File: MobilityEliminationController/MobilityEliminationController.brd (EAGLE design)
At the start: 57.1 x 63.5 mm, 94 parts, among them Q1 INFINEON_2N7002_DW, Q2 INFINEON_2N7002_DW, Q3 BS250F, Q4 BS250F, Q5 INFINEON_2N7002_DW, Q6 INFINEON_2N7002_DW, U1 MSP430F5521/5/7/9_PN80, U2 SN74LV74, U3 SN74LV08

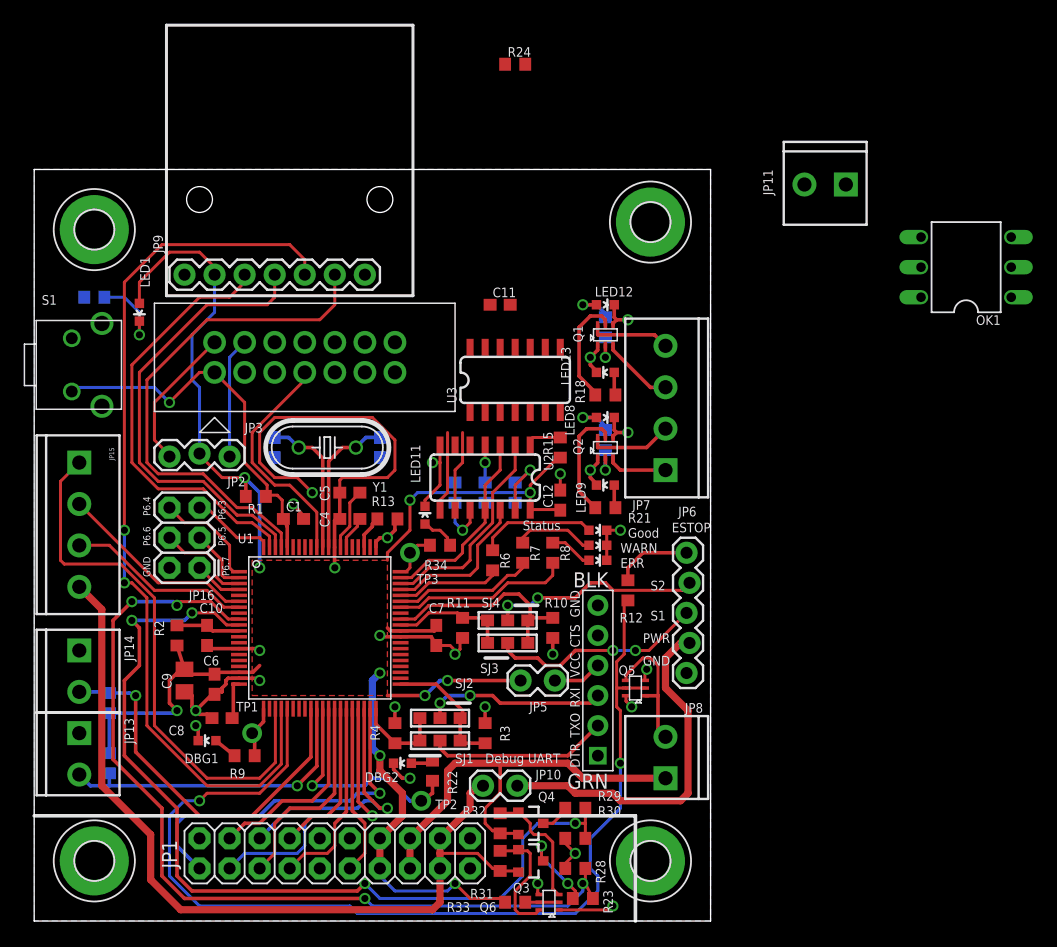
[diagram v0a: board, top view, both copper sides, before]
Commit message: Mob/Elim controller ready for fab
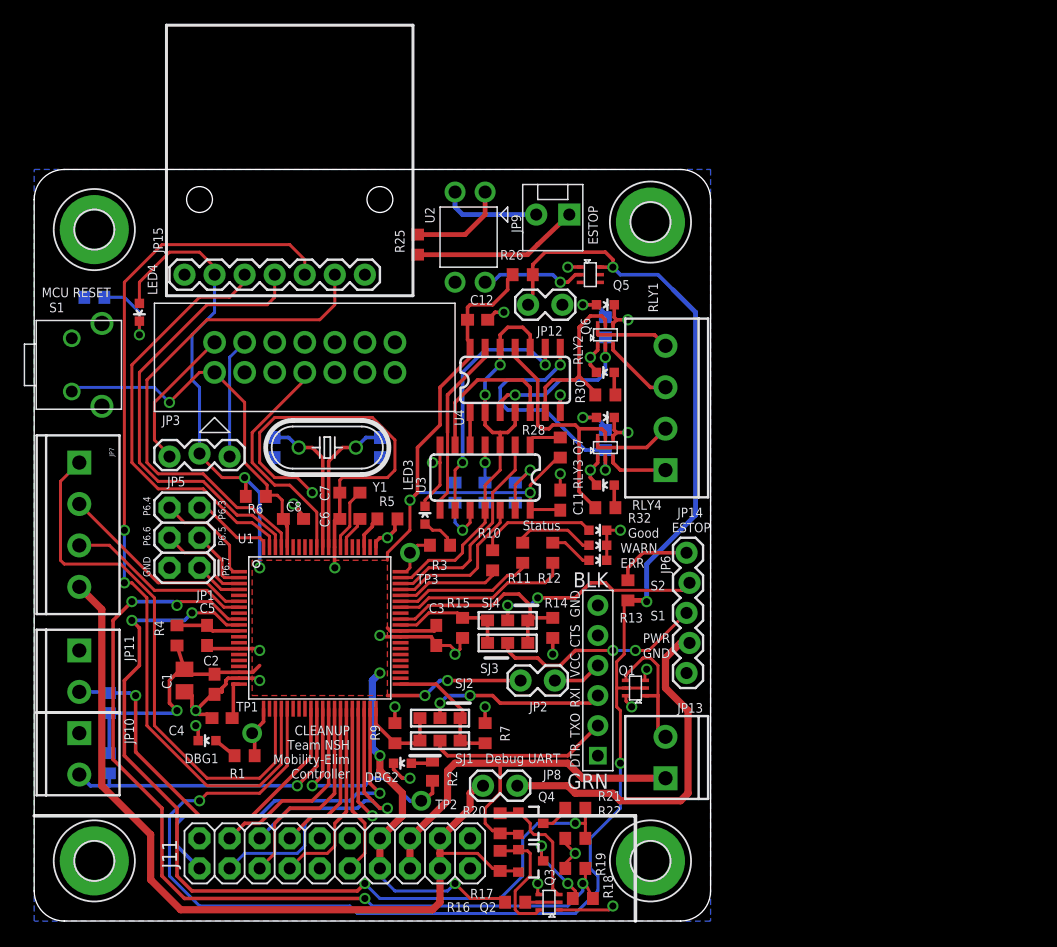
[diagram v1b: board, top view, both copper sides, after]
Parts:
- removed JP16: (no value), SparkFun-Connectors:2X3
- removed LED12, LED13: (no value), SparkFun-LED:LED-0603
- removed OK1: 4N35, optocoupler:DIL06
- removed R35: 1k, rcl:R0603
- added J11: M10X2, SparkFun-Connectors:2X10
- added JP12: M02LOCK, SparkFun-Connectors:1X02_LOCK
- added LED6: Status: Yellow, SparkFun-LED:LED-0603
- added LED7: Status: Red, SparkFun-LED:LED-0603
- added Q7: INFINEON_2N7002_DW, npol-discrete:INFINEON_SOT363
- added R19: 100k, rcl:R0603
- added R25: 620, rcl:R0603
- added U4: SN74LV08, npol-digital:TI_D_R-PDSO-G14_SOIC14
- C1: value 1nF -> 10uF; device rcl:C0603 -> rcl:C0805
- C10: value 0.1uF -> 1nF
- C2, C3: value 1nF -> 0.1uF
- C4: value 220nF -> 470nF
- C5: value 220nF -> 0.1uF
- C6, C7: value 0.1uF -> 220nF
- C8: value 470nF -> 1nF
- C9: value 10uF -> 1nF; device rcl:C0805 -> rcl:C0603
- JP1: value M10X2 -> (none); device SparkFun-Connectors:2X10 -> SparkFun-Connectors:2X3
- JP10: value M02LOCK -> M023.5MM; device SparkFun-Connectors:1X02_LOCK -> SparkFun-Connectors:SCREWTERMINAL-3.5MM-2
- JP14: value M023.5MM -> (none); device SparkFun-Connectors:SCREWTERMINAL-3.5MM-2 -> SparkFun-Connectors:SCREWTERMINAL-3.5MM-4
- JP15: device SparkFun-Connectors:SCREWTERMINAL-3.5MM-4 -> SparkFun-Connectors:1X07
- JP2: value (none) -> M02LOCK; device SparkFun-Connectors:1X03_LOCK -> SparkFun-Connectors:1X02_LOCK
- JP5: value M02LOCK -> (none); device SparkFun-Connectors:1X02_LOCK -> SparkFun-Connectors:1X03_LOCK
- JP8: value M023.5MM -> M02LOCK; device SparkFun-Connectors:SCREWTERMINAL-3.5MM-2 -> SparkFun-Connectors:1X02_LOCK
- JP9: value (none) -> M02POLAR_LOCK; device SparkFun-Connectors:1X07 -> SparkFun-Connectors:MOLEX-1X2_LOCK
- LED1: value 3V3 OK -> Status: Red
- LED10, LED11: value Status: Red -> (none)
- LED2: value Status: Green -> Status: Red
- LED3: value Status: Yellow -> Status: Red
- LED4: value Status: Red -> 3V3 OK
- LED5: value Status: Red -> Status: Green
- R1: value 47k -> 330
- R10, R11, R3: value 10k -> 330
- R12, R2: value 0 -> 330
- R13: value 1M -> 0
- R14, R15, R16, R17: value 0 -> 10k
- R18, R21: value 1k -> 100k
- R20: value 1k -> 10k
- R22, R7, R9: value 330 -> 10k
- R23: value 100k -> 10k
- R24: value 620 -> 10k
- R27, R33, R4: value 10k -> 0
- R28: value 100k -> 0
- R29: value 100k -> 1k
- R30, R31, R32: value 10k -> 1k
- R34: value 330 -> 0
- R5: value 330 -> 1M
- R6: value 330 -> 47k
- U2: value SN74LV74 -> LTV-817; device npol-digital:TI_D_R-PDSO-G14_SOIC14 -> npol-digital:LITEON_DIL04_.3
- U3: value SN74LV08 -> SN74LV74
- moved JP11 75.8 mm to (3.81, 22.9), turned to 270 degrees
- moved R24 63.9 mm to (6.35, 18.4), flipped to the bottom, turned to 270 degrees
- moved R26 54.1 mm to (41.3, 54.6), flipped to the top, turned to 0 degrees
- moved JP14 51.8 mm to (53.3, 38.1), turned to 90 degrees
- moved JP13 49.7 mm to (53.3, 12.1), turned to 90 degrees
- moved JP7 49.5 mm to (3.81, 38.7), turned to 270 degrees
- moved Q6 48.2 mm to (48.3, 49.5), turned to 0 degrees
- moved R8 44.3 mm to (5.08, 52.7), flipped to the bottom, turned to 180 degrees
- moved LED4 44.0 mm to (8.89, 51.4), turned to 180 degrees
- moved R18 42.6 mm to (46.4, 1.91)
- moved R23 41.6 mm to (6.35, 13.3), flipped to the bottom, turned to 90 degrees
- moved R29 40.7 mm to (48.3, 50.2), flipped to the bottom, turned to 270 degrees
- moved Q2 38.7 mm to (43.5, 1.59), turned to 90 degrees
- moved R30 37.6 mm to (48.3, 44.5), turned to 180 degrees
- moved LED5 37.5 mm to (47.6, 33.0), turned to 270 degrees
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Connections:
- removed net N$38: OK1.1, R24.1
- new net ESTOP_LOCAL_INV: Q5.2, U2.4
- net +12V: now also J11.15, J11.16, JP13.1, R20.2; no longer JP1.15, JP1.16, JP8.1, R32.2
- net +3V3: now also C1.1, C2.1, C3.1, J11.13, J11.14, JP15.2, JP2.1, JP5.2, LED4.A, R23.2, R24.2, R26.1, R28.1, R34.1, R4.2, R6.2, U4.14; no longer C6.1, C7.1, C9.1, JP1.13, JP1.14, JP2.2, JP5.1, JP9.2, LED1.A, R1.2, R14.2, R15.1, R17.1, R2.2, R26.2, U2.14
- net +5V: now also J11.17, J11.18, JP7.4, JP8.2, R17.2; no longer JP1.17, JP1.18, JP10.2, JP15.4, R31.2
- net 12VSENSE: now also R21.1, R22.2; no longer R29.1, R30.2
- net 5VSENSE: now also R18.1, R19.2; no longer R23.1, R28.2
- net AVCC: now also C5.1, R4.1; no longer C10.1, R2.1
- net CAN_/CS: now also J11.4; no longer JP1.4
- net CAN_/INT: now also J11.5; no longer JP1.5
- net CAN_/RESET: now also J11.2; no longer JP1.2
- net CAN_/RX0BF: now also J11.8; no longer JP1.8
- net CAN_/RX1BF: now also J11.7; no longer JP1.7
- net CAN_/TX0RTS: now also J11.12; no longer JP1.12
- net CAN_/TX1RTS: now also J11.9; no longer JP1.9
- net CAN_/TX2RTS: now also J11.10; no longer JP1.10
- net CAN_MISO: now also J11.6; no longer JP1.6
- net CAN_MOSI: now also J11.3; no longer JP1.3
- net CAN_SCK: now also J11.1; no longer JP1.1
- net CAN_STBY: now also J11.11; no longer JP1.11
- net DBG_LED1: now also R1.2; no longer R9.2
- net DBG_LED2: now also R2.2; no longer R22.2
- net DBG_LED3: now also R3.2; no longer R34.2
- net DBG_RXD: now also R7.2; no longer R3.2
- net DBG_TXD: now also R9.2; no longer R4.2
- net DRILL_EN: now also U3.11, U3.3, U4.10, U4.12, U4.2, U4.4; no longer U2.11, U2.3, U3.10, U3.12, U3.2, U3.4
- net DRILL_ISENSE_/FAULT: now also JP15.5; no longer JP9.5
- net DRILL_ISENSE_FAULT_EN: now also JP15.6; no longer JP9.6
- net DRILL_ISENSE_VIOUT: now also JP15.3; no longer JP9.3
- net DRILL_ISENSE_VZCR: now also JP15.4; no longer JP9.4
- net DRILL_RELAY_1: now also JP14.4, Q6.6; no longer JP7.4, Q1.6
- net DRILL_RELAY_2: now also JP14.3, Q6.3; no longer JP7.3, Q1.3
- net DRILL_RELAY_3: now also JP14.2, Q7.6; no longer JP7.2, Q2.6
- net DRILL_RELAY_4: now also JP14.1, Q7.3; no longer JP7.1, Q2.3
- net DRILL_S1: now also U3.2; no longer U2.2
- net DRILL_S2: now also U3.12; no longer U2.12
- net ESTOP+: now also JP9.1, R25.2; no longer JP11.2, R24.2
- net ESTOP-: now also JP9.2, U2.2; no longer JP11.1, OK1.2
- net ESTOP_LOCAL: now also JP12.1, Q1.2, Q1.5, Q5.6, R13.1, R26.2; no longer Q5.2, Q5.5, R12.1
- net ESTOP_RELAY: now also JP13.2, Q1.1, Q1.4; no longer JP8.2, Q5.1, Q5.4
- net GND: now also J11.19, J11.20, JP1.2, JP10.1, JP11.1, JP12.2, JP15.1, LED1.C, LED6.C, LED7.C, Q1.3, Q1.6, Q5.1, Q7.1, Q7.4, R14.1, R15.1, R19.1, R22.1, R7.1, R8.1, R9.1, U2.3, U4.7; no longer JP1.19, JP1.20, JP13.1, JP14.1, JP16.2, JP9.1, LED12.C, LED13.C, LED4.C, OK1.4, Q1.1, Q1.4, Q5.3, Q5.6, R10.1, R11.1, R13.1, R28.1, R3.1, R30.1, R4.1, U2.7
- net LOWER_SWITCH: now also JP11.2, R24.1; no longer JP14.2, R27.1
- net N$1: now also JP2.2; no longer JP5.2
- net N$10: now also Q2.6, R17.1; no longer Q6.6, R31.1
- net N$11: now also R21.2; no longer R29.2
- net N$12: now also Q2.2, Q2.5, R16.1; no longer Q6.2, Q6.5, R33.1
- net N$13: now also R25.1, U2.1; no longer OK1.5
- net N$14: now also LED9.A, R30.1; no longer LED13.A, R18.1
- net N$2: now also LED4.C, R8.2; no longer LED1.C, R5.2
- net N$20: now also U3.5, U4.1; no longer U2.5, U3.1
- net N$22: now also U3.6, U4.5; no longer U2.6, U3.5
- net N$23: now also U4.9; no longer U2.9
- net N$25: now also U3.8, U4.13; no longer U2.8, U3.13
- net N$26: now also R27.1, U3.4; no longer R14.1, U2.4
- net N$27: now also R28.2, U3.1; no longer R15.2, U2.1
- net N$28: now also R33.1, U3.10; no longer R16.1, U2.10
- net N$29: now also R34.2, U3.13; no longer R17.2, U2.13
- net N$3: now also LED5.A, R10.1; no longer LED2.A, R6.1
- net N$33: now also LED11.A, R32.1; no longer LED9.A, R21.1
- net N$36: now also LED3.A, R3.1; no longer LED11.A, R34.1
- net N$4: now also LED6.A, R11.1; no longer LED3.A, R7.1
- net N$5: now also LED7.A, R12.1; no longer LED4.A, R8.1
- net N$6: now also LED1.A, R1.1; no longer LED5.A, R9.1
- net N$7: now also R5.2; no longer R13.2
- net N$8: now also LED2.A, R2.1; no longer LED10.A, R22.1
- net N$9: now also R18.2; no longer R23.2
- net NU_P6.3: now also JP1.5; no longer JP16.5
- net NU_P6.4: now also JP1.6; no longer JP16.6
- net NU_P6.5: now also JP1.3; no longer JP16.3
- net NU_P6.6: now also JP1.4; no longer JP16.4
- net NU_P6.7: now also JP1.1; no longer JP16.1
- net RC_PWR: now also JP8.1; no longer JP10.1
- net RC_RXD: now also R14.2; no longer R10.2
- net RC_S3: now also R13.2; no longer R12.2
- net RC_TXD: now also R15.2; no longer R11.2
- net RELAY1_CNTRL: now also Q6.2, R29.2, U4.3; no longer Q1.2, R35.2, U3.3
- net RELAY1_LED_A: now also LED8.A, R29.1; no longer LED12.A, R35.1
- net RELAY2_CNTRL: now also Q6.5, R30.2, U4.6; no longer Q1.5, R18.2, U3.6
- net RELAY3_CNTRL: now also Q7.2, R31.2, U4.8; no longer Q2.2, R20.2, U3.8
- net RELAY3_LED_A: now also LED10.A, R31.1; no longer LED8.A, R20.1
- net RELAY4_CNTRL: now also Q7.5, R32.2, U4.11; no longer Q2.5, R21.2, U3.11
- net SBWTDIO: now also C8.1, R6.1; no longer C1.1, R1.1
- net STAT_ERR: now also R12.2; no longer R8.2
- net STAT_OK: now also R10.2; no longer R6.2
- net STAT_WARN: now also R11.2; no longer R7.2
- net STEPPER_DIR: now also JP7.2; no longer JP15.2
- net STEPPER_EN: now also JP7.3; no longer JP15.3
- net STEPPER_STEP: now also JP7.1; no longer JP15.1
- net UPPER_SWITCH: now also JP10.2, R23.1; no longer JP13.2, R26.1
- net V18: now also C7.1; no longer C5.1
- net VCC_TARGET: now also JP5.1; no longer JP2.1
- net VCC_TOOL: now also JP5.3; no longer JP2.3
- net VCORE: now also C4.1; no longer C8.1
- net VOC: now also JP15.7; no longer JP9.7
- net VTAP_EN: now also Q2.3, R20.1; no longer Q6.3, R32.1
- net VUSB: now also C6.1; no longer C4.1
- net XT2IN: now also C9.1; no longer C2.1
- net XT2OUT: now also C10.1; no longer C3.1
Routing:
- net ESTOP_LOCAL: track 89.1 -> 138.2 mm, vias 2 -> 4
- net +3V3: track 138.2 -> 162.1 mm
- net RELAY3_CNTRL: track 2.79 -> 21.9 mm, vias 1 -> 2
- net DRILL_EN: track 16.5 -> 34.1 mm, vias 0 -> 2
- net N$23: track 6.77 -> 21.6 mm, vias 0 -> 2
- net ESTOP+: track 0.00 -> 14.2 mm
- net RELAY1_CNTRL: track 1.10 -> 14.8 mm, vias 1 -> 2
- net N$22: track 0.00 -> 13.1 mm
- net RELAY4_CNTRL: track 9.69 -> 21.2 mm
- net ESTOP_LOCAL_INV: track 0.00 -> 8.88 mm, vias 0 -> 1
- net N$25: track 6.77 -> 15.2 mm
- net ESTOP-: track 0.00 -> 8.39 mm
- net N$13: track 0.00 -> 8.32 mm
- net RELAY2_CNTRL: track 9.50 -> 14.8 mm
- net GND: track 107.3 -> 111.5 mm, vias 26 -> 29
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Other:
- outline, holes or cut-outs redrawn
- board text added: "CLEANUP Team NSH Mobility-Elim Controller"
- board text added: "MCU RESET"
- board text added: "RLY1"
- board text added: "RLY2"
- board text added: "RLY3"
- board text added: "RLY4"
